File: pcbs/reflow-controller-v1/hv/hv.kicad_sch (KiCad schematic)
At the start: 7 parts, among them J101 EB163A-03-C-180, J102 EB163A-02-C-180, J103 EB163A-02-C-180, J104 EB163A-02-C-180, J105 EB163A-02-C-180

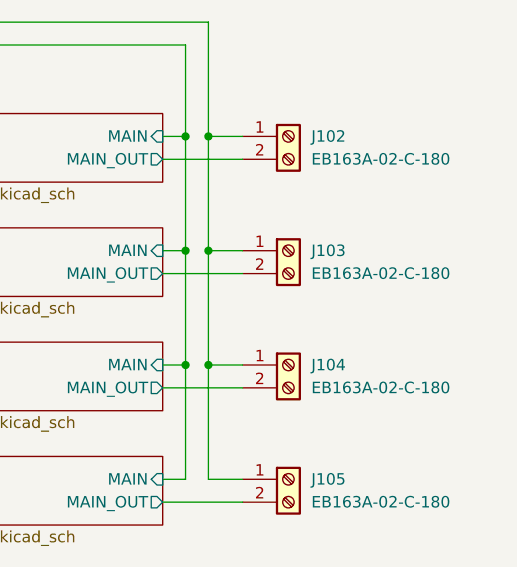
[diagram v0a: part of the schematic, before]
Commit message: Initial hv placing
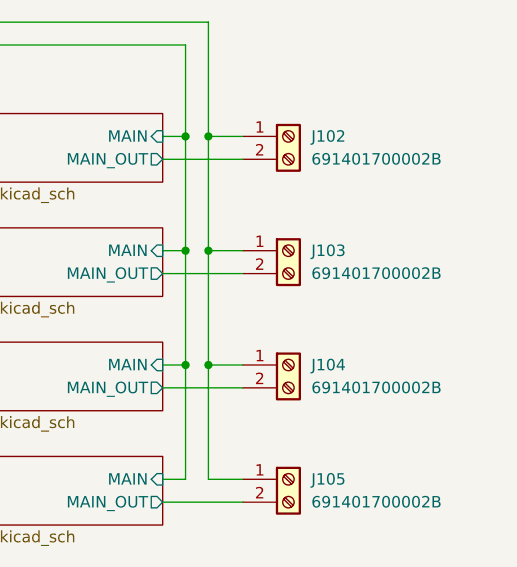
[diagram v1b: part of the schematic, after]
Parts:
- J102, J103, J104, J105: value EB163A-02-C-180 -> 691401700002B; footprint Connector_Phoenix_SPT:PhoenixContact_SPT_2.5_2-V-5.0-EX_1x02_P5.0mm_Vertical -> wuerth:691401700002B
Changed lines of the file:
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@@
-		)
-	)
-	(netclass_flag ""
-		(length 2.54)
-		(shape round)
-		(at 246.38 20.32 0)
-		(fields_autoplaced yes)
-		(effects
-			(font
-				(size 1.27 1.27)
-			)
-			(justify left bottom)
-		)
-		(property "Netclass" "Default"
-			(at 247.0785 17.78 0)
-			(effects
-				(font
-					(size 1.27 1.27)
-				)
-				(justify left)
-			)
-		)
-		(property "Component Class" ""
-			(at -53.34 -26.67 0)
-			(effects
-				(font
-					(size 1.27 1.27)
-					(italic yes)
-				)
-			)
 		)
 	)
@@
 		(on_board yes)
 		(dnp no)
-		(fields_autoplaced yes)
 		(property "Reference" "J102"
 			(at 260.35 40.64 0)
@@
 			)
 		)
-		(property "Value" "EB163A-02-C-180"
+		(property "Value" "691401700002B"
 			(at 260.35 43.18 0)
 			(effects
@@
 			)
 		)
-		(property "Footprint" "Connector_Phoenix_SPT:PhoenixContact_SPT_2.5_2-V-5.0-EX_1x02_P5.0mm_Vertical"
+		(property "Footprint" "wuerth:691401700002B"
 			(at 257.81 40.64 0)
 			(effects
@@
 		(on_board yes)
 		(dnp no)
-		(fields_autoplaced yes)
 		(property "Reference" "J103"
 			(at 260.35 53.34 0)
@@
 			)
 		)
-		(property "Value" "EB163A-02-C-180"
+		(property "Value" "691401700002B"
 			(at 260.35 55.88 0)
 			(effects
@@
 			)
 		)
-		(property "Footprint" "Connector_Phoenix_SPT:PhoenixContact_SPT_2.5_2-V-5.0-EX_1x02_P5.0mm_Vertical"
+		(property "Footprint" "wuerth:691401700002B"
 			(at 257.81 53.34 0)
 			(effects
@@
 		(on_board yes)
 		(dnp no)
-		(fields_autoplaced yes)
 		(property "Reference" "J105"
 			(at 260.35 78.74 0)
@@
 			)
 		)
-		(property "Value" "EB163A-02-C-180"
+		(property "Value" "691401700002B"
 			(at 260.35 81.28 0)
 			(effects
@@
 			)
 		)
-		(property "Footprint" "Connector_Phoenix_SPT:PhoenixContact_SPT_2.5_2-V-5.0-EX_1x02_P5.0mm_Vertical"
+		(property "Footprint" "wuerth:691401700002B"
 			(at 257.81 78.74 0)
 			(effects
@@
 		(on_board yes)
 		(dnp no)
-		(fields_autoplaced yes)
 		(property "Reference" "J104"
 			(at 260.35 66.04 0)
@@
 			)
 		)
-		(property "Value" "EB163A-02-C-180"
+		(property "Value" "691401700002B"
 			(at 260.35 68.58 0)
 			(effects
@@
 			)
 		)
-		(property "Footprint" "Connector_Phoenix_SPT:PhoenixContact_SPT_2.5_2-V-5.0-EX_1x02_P5.0mm_Vertical"
+		(property "Footprint" "wuerth:691401700002B"
 			(at 257.81 66.04 0)
 			(effects

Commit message: improve component selection
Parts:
- F101, F102: value Schurter 0031.8221 -> Würth 696103101002; footprint Fuse:Fuseholder_Cylinder-5x20mm_Schurter_OGN-SMD_Horizontal_Open -> Fuse:Fuseholder_Cylinder-5x20mm_Wuerth_696103101002-SMD_Horizontal_Open
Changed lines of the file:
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@@
 			)
 		)
-		(property "Value" "Schurter 0031.8221"
+		(property "Value" "Würth 696103101002"
 			(at 69.85 33.02 90)
 			(effects
@@
 			)
 		)
-		(property "Footprint" "Fuse:Fuseholder_Cylinder-5x20mm_Schurter_OGN-SMD_Horizontal_Open"
+		(property "Footprint" "Fuse:Fuseholder_Cylinder-5x20mm_Wuerth_696103101002-SMD_Horizontal_Open"
 			(at 69.85 37.338 90)
 			(effects
@@
 			)
 		)
-		(property "Value" "Schurter 0031.8221"
+		(property "Value" "Würth 696103101002"
 			(at 69.85 45.72 90)
 			(effects
@@
 			)
 		)
-		(property "Footprint" "Fuse:Fuseholder_Cylinder-5x20mm_Schurter_OGN-SMD_Horizontal_Open"
+		(property "Footprint" "Fuse:Fuseholder_Cylinder-5x20mm_Wuerth_696103101002-SMD_Horizontal_Open"
 			(at 69.85 42.418 90)
 			(effects

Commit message: route hv pcb
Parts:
- added H101, H102, H103: MountingHole_Pad, Mounting_Wuerth:Mounting_Wuerth_WA-SMSR-3.2mm_H5.1mm_ReverseMount_9775051960, symbol Mechanical:MountingHole_Pad
- J101: value EB163A-03-C-180 -> 691401700003B; footprint Connector_Phoenix_SPT:PhoenixContact_SPT_2.5_3-V-5.0-EX_1x03_P5.0mm_Vertical -> wuerth:691401700003B
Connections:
- net Earth_Protective: now also H101.1, H102.1
- new net GND: H103.1
